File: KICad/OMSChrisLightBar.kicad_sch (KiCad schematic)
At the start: 25 parts, among them U1 NodeMCU_1.0_(ESP-12E)

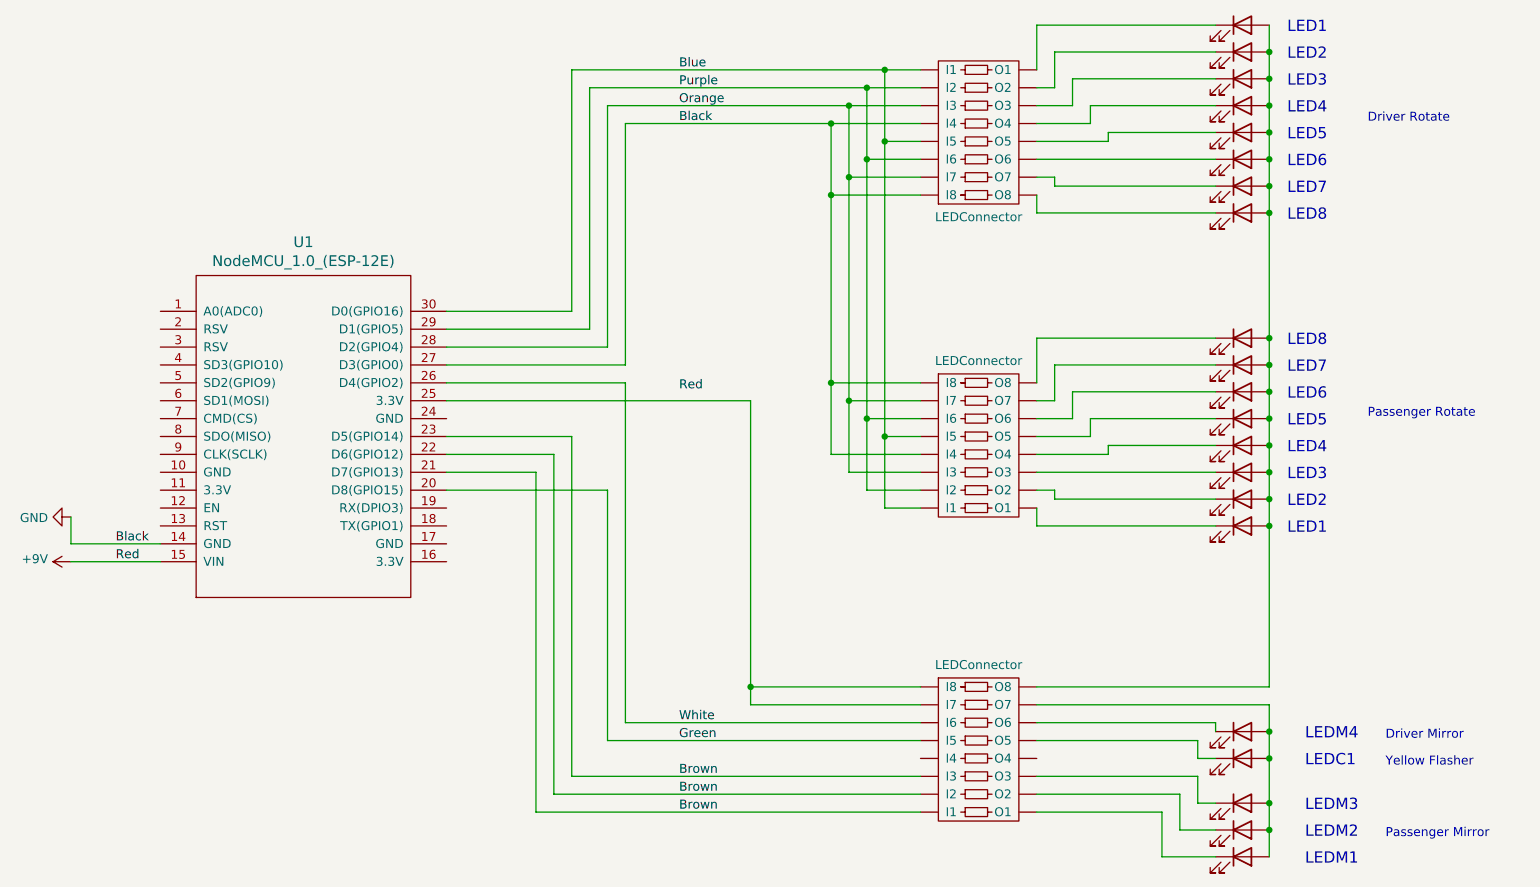
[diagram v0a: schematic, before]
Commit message: Changed passenger mirror direction
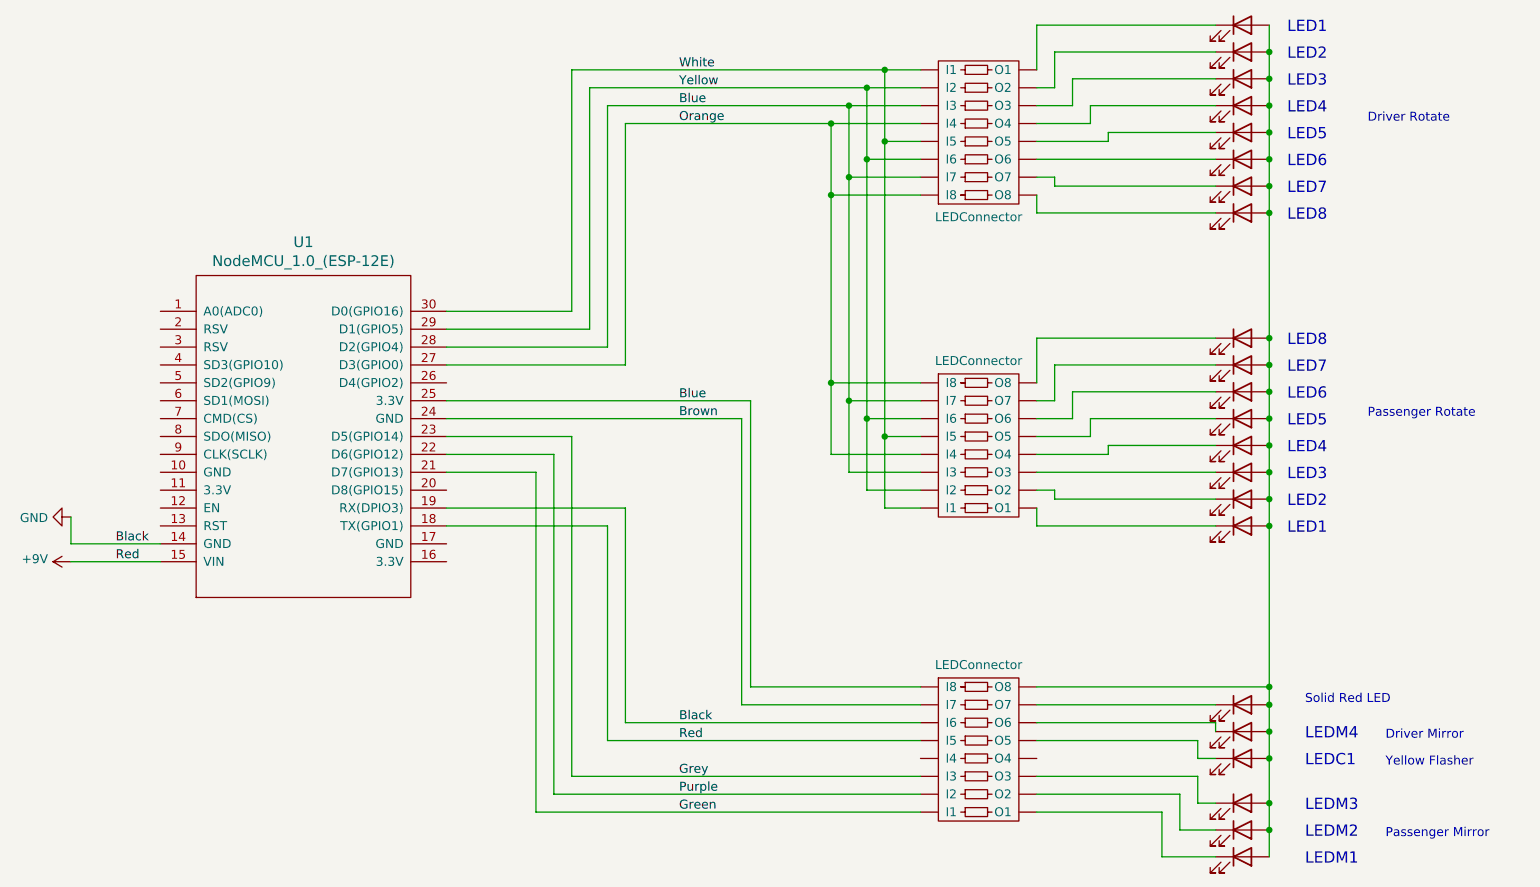
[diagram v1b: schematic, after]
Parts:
- added D?: LED, symbol Device:LED
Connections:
- net +9V: now also LU3.~ (O8), U1.18 (TX(GPIO1))
- net Blue: now also LU3.~ (O8), U1.25 (3.3V), U1.28 (D2(GPIO4)); no longer U1.30 (D0(GPIO16))
- net Brown: now also U1.24 (GND); no longer U1.21 (D7(GPIO13)), U1.22 (D6(GPIO12)), U1.23 (D5(GPIO14))
- net GND: now also LU3.~ (O8), U1.19 (RX(DPIO3)); no longer LU1.~ (O8), LU?.~ (O8), U1.27 (D3(GPIO0))
- net Green: now also U1.21 (D7(GPIO13)); no longer U1.20 (D8(GPIO15))
- net Orange: now also U1.27 (D3(GPIO0)); no longer U1.28 (D2(GPIO4))
- net Purple: now also LU3.~ (O8), U1.22 (D6(GPIO12)); no longer LU1.~ (O8), LU?.~ (O8), U1.29 (D1(GPIO5))
- net White: now also LU1.~ (O8), LU?.~ (O8), U1.30 (D0(GPIO16)); no longer LU3.~ (O8), U1.26 (D4(GPIO2))
- net at D?.2 (A), D?.2 (A), D?.2 (A)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: now also D?.2 (A), D?.2 (A), D?.2 (A), D?.2 (A), D?.2 (A), D?.2 (A)
- new net: D?.1 (K), LU3.~ (O8)
- new net Grey: LU3.~ (O8), U1.23 (D5(GPIO14))
- new net Yellow: LU1.~ (O8), LU?.~ (O8), U1.29 (D1(GPIO5))
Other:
- note added: "Solid Red LED"
